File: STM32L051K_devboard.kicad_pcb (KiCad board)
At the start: 2 copper layers, 20.7 x 54.2 mm, 50 parts, among them J1 Conn_01x16_Pin, J2 Conn_01x16_Pin, J3 Conn_01x05_Pin, U1 STM32L051K8Ux

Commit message: cambios minimos
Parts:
- removed kibuzzard-69C45A72: G***, kibuzzard-69C45A72
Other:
- board text added: "STM32L051K8U"
- board text added: "X"

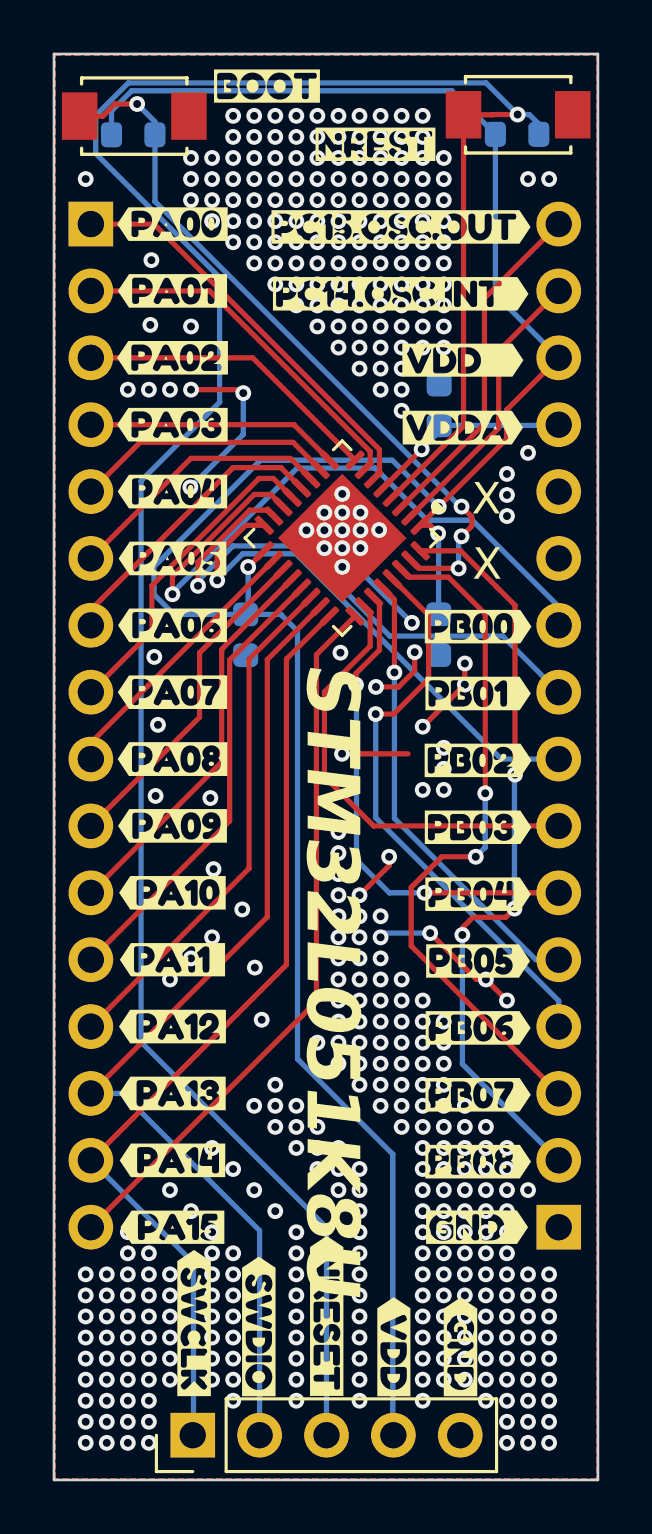
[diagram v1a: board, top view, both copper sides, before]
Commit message: Agregado XTAL low power y pines clock removidos
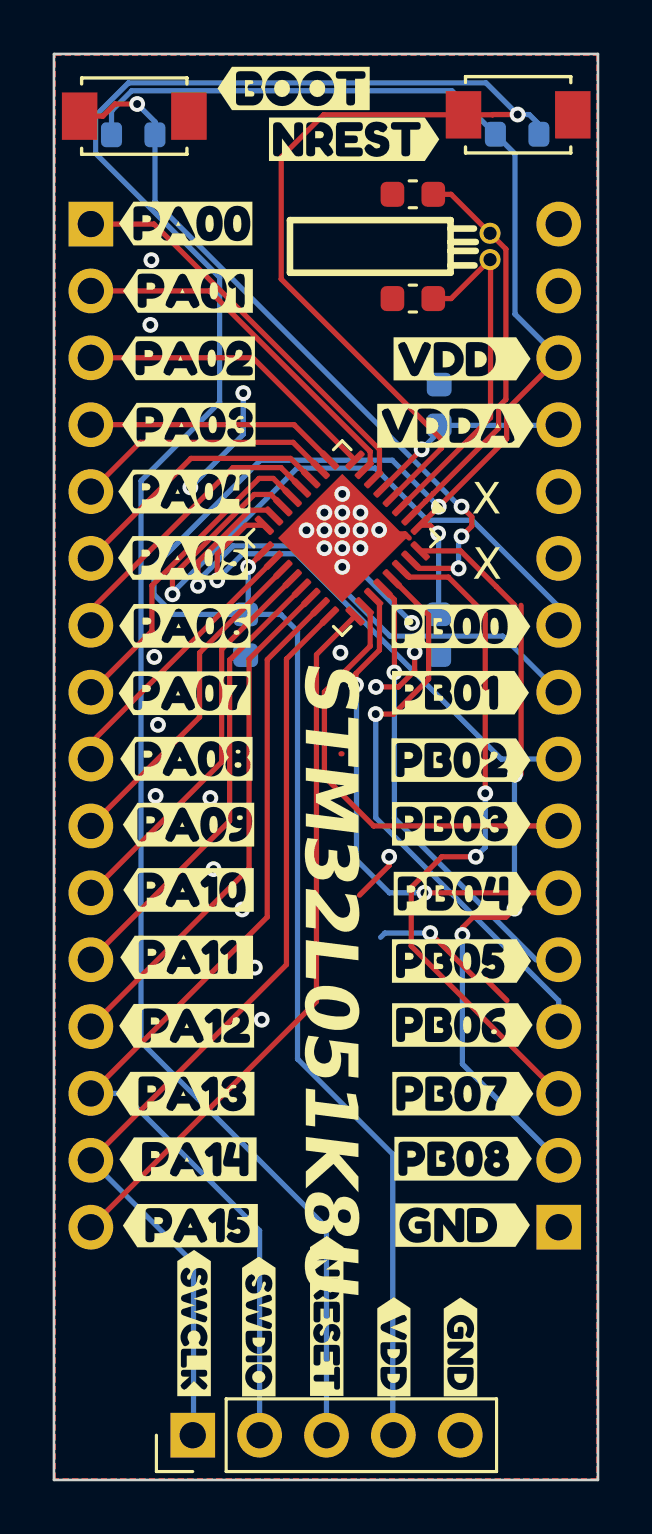
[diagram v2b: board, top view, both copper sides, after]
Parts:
- removed G***: LOGO, Images:LOGOv3.4
- removed kibuzzard-69C44E8F: G***, kibuzzard-69C44E8F
- removed kibuzzard-69C44ECA: G***, kibuzzard-69C44ECA
- removed kibuzzard-69C44EF4: G***, kibuzzard-69C44EF4
- removed kibuzzard-69C44F15: G***, kibuzzard-69C44F15
- removed kibuzzard-69C44F1D: G***, kibuzzard-69C44F1D
- removed kibuzzard-69C44F22: G***, kibuzzard-69C44F22
- removed kibuzzard-69C44F28: G***, kibuzzard-69C44F28
- removed kibuzzard-69C44FA1: G***, kibuzzard-69C44FA1
- removed kibuzzard-69C44FA7: G***, kibuzzard-69C44FA7
- removed kibuzzard-69C44FAD: G***, kibuzzard-69C44FAD
- removed kibuzzard-69C44FBD: G***, kibuzzard-69C44FBD
- removed kibuzzard-69C44FDE: G***, kibuzzard-69C44FDE
- removed kibuzzard-69C44FFF: G***, kibuzzard-69C44FFF
- removed kibuzzard-69C45005: G***, kibuzzard-69C45005
- removed kibuzzard-69C4500C: G***, kibuzzard-69C4500C
- removed kibuzzard-69C45011: G***, kibuzzard-69C45011
- removed kibuzzard-69C4505F: G***, kibuzzard-69C4505F
- removed kibuzzard-69C4508C: G***, kibuzzard-69C4508C
- removed kibuzzard-69C450DF: G***, kibuzzard-69C450DF
- removed kibuzzard-69C450F7: G***, kibuzzard-69C450F7
- removed kibuzzard-69C450FE: G***, kibuzzard-69C450FE
- removed kibuzzard-69C45105: G***, kibuzzard-69C45105
- removed kibuzzard-69C4510A: G***, kibuzzard-69C4510A
- removed kibuzzard-69C45110: G***, kibuzzard-69C45110
- removed kibuzzard-69C45115: G***, kibuzzard-69C45115
- removed kibuzzard-69C451D3: G***, kibuzzard-69C451D3
- removed kibuzzard-69C451DA: G***, kibuzzard-69C451DA
- removed kibuzzard-69C45252: G***, kibuzzard-69C45252
- removed kibuzzard-69C45274: G***, kibuzzard-69C45274
- removed kibuzzard-69C45C41: G***, kibuzzard-69C45C41
- removed kibuzzard-69C45C6A: G***, kibuzzard-69C45C6A
- removed kibuzzard-69C474E9: G***, kibuzzard-69C474E9
- added C1: 12pF, Capacitor_SMD:C_0603_1608Metric, F.Cu at (143.2, 77.4)
- added C2: 12pF, Capacitor_SMD:C_0603_1608Metric, F.Cu at (143.2, 73.5)
- added X1: TAXD32768K2BGBBZT2S, EasyEDA:OSC-TH_BD2.0-P0.70-D0.3, F.Cu at (146.1, 75.4)
- added kibuzzard-6A013291: G***, kibuzzard-6A013291, F.Cu at (134.5, 87.3)
- added kibuzzard-6A0132A3: G***, kibuzzard-6A0132A3, F.Cu at (134.5, 84.7)
- added kibuzzard-6A0132D3: G***, kibuzzard-6A0132D3, F.Cu at (134.6, 74.6)
- added kibuzzard-6A0132E0: G***, kibuzzard-6A0132E0, F.Cu at (134.7, 77.1)
- added kibuzzard-6A0132F9: G***, kibuzzard-6A0132F9, F.Cu at (134.7, 79.7)
- added kibuzzard-6A01330E: G***, kibuzzard-6A01330E, F.Cu at (134.7, 82.2)
- added kibuzzard-6A013338: G***, kibuzzard-6A013338, F.Cu at (134.5, 89.8)
- added kibuzzard-6A01335E: G***, kibuzzard-6A01335E, F.Cu at (134.5, 92.4)
- added kibuzzard-6A0133A5: G***, kibuzzard-6A0133A5, F.Cu at (134.6, 94.9)
- added kibuzzard-6A0133D4: G***, kibuzzard-6A0133D4, F.Cu at (134.7, 97.4)
- added kibuzzard-6A0133F3: G***, kibuzzard-6A0133F3, F.Cu at (134.7, 99.9)
- added kibuzzard-6A013428: G***, kibuzzard-6A013428, F.Cu at (134.6, 102.4)
- added kibuzzard-6A013453: G***, kibuzzard-6A013453, F.Cu at (134.6, 105.0)
- added kibuzzard-6A01346E: G***, kibuzzard-6A01346E, F.Cu at (134.6, 107.6)
- added kibuzzard-6A01348C: G***, kibuzzard-6A01348C, F.Cu at (134.7, 110.1)
- added kibuzzard-6A013498: G***, kibuzzard-6A013498, F.Cu at (134.8, 112.6)
- added kibuzzard-6A0134D7: G***, kibuzzard-6A0134D7, F.Cu at (145.1, 110.1)
- added kibuzzard-6A013521: G***, kibuzzard-6A013521, F.Cu at (138.7, 69.4)
- added kibuzzard-6A01353B: G***, kibuzzard-6A01353B, F.Cu at (141.0, 71.4)
- added kibuzzard-6A013575: G***, kibuzzard-6A013575, F.Cu at (145.1, 112.6)
- added kibuzzard-6A013597: G***, kibuzzard-6A013597, F.Cu at (145.1, 107.6)
- added kibuzzard-6A0135B5: G***, kibuzzard-6A0135B5, F.Cu at (145.1, 105.0)
- added kibuzzard-6A0135C4: G***, kibuzzard-6A0135C4, F.Cu at (145.1, 102.6)
- added kibuzzard-6A0135ED: G***, kibuzzard-6A0135ED, F.Cu at (145.0, 97.4)
- added kibuzzard-6A0135F3: G***, kibuzzard-6A0135F3, F.Cu at (145.1, 100.0)
- added kibuzzard-6A013611: G***, kibuzzard-6A013611, F.Cu at (145.0, 94.9)
- added kibuzzard-6A01362E: G***, kibuzzard-6A01362E, F.Cu at (145.0, 92.4)
- added kibuzzard-6A01363E: G***, kibuzzard-6A01363E, F.Cu at (145.0, 89.9)
- added kibuzzard-6A01366B: G***, kibuzzard-6A01366B, F.Cu at (144.8, 82.2)
- added kibuzzard-6A0136A4: G***, kibuzzard-6A0136A4, F.Cu at (145.1, 79.7)
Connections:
- J2 pad 15: /PC14_OSC.INT -> unconnected-(J2-Pin_15-Pad15)
- J2 pad 16: /PC15_OSC.OUT -> unconnected-(J2-Pin_16-Pad16)
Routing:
- net /NRST: track 92.3 -> 100.5 mm
- net GND: track 26.0 -> 20.6 mm, vias 426 -> 31
- net /PC14_OSC.INT: track 10.9 -> 15.3 mm
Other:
- board text added: "32.768 kHz"

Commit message: agregado LDO y VDDA puenteado a 3.3
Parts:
- removed kibuzzard-6A01366B: G***, kibuzzard-6A01366B
- removed kibuzzard-6A0136A4: G***, kibuzzard-6A0136A4
- added U2: XC6206P332MR, EasyEDA:SOT-23-3_L2.9-W1.6-P1.90-LS2.8-BR, B.Cu at (142.4, 75.7)
- added kibuzzard-6A120E41: G***, kibuzzard-6A120E41, F.Cu at (145.3, 82.2)
- added kibuzzard-6A120E83: G***, kibuzzard-6A120E83, F.Cu at (145.3, 79.7)
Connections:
- C4 pad 1: /VDDA -> /VDD0
- J2 pad 13: /VDDA -> /LDO
- U1 pad 5: /VDDA -> /VDD0
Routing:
- net /VDD0: track 93.8 -> 103.7 mm, vias 3 -> 4
- net /LDO: track 0.00 -> 8.62 mm
- net /VDDA: track 7.82 -> 0.00 mm, vias 1 -> 0
- net GND: vias 31 -> 277

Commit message: cambio de crital a SMD 8 MHz
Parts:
- removed X1: TAXD32768K2BGBBZT2S, EasyEDA:OSC-TH_BD2.0-P0.70-D0.3
- removed kibuzzard-6A013575: G***, kibuzzard-6A013575
- added D1: LED_Small, LED_SMD:LED_0603_1608Metric, F.Cu at (140.7, 79.5)
- added D2: LED_Small, LED_SMD:LED_0603_1608Metric, F.Cu at (131.8, 115.9)
- added JP1: SolderJumper_2_Open, Jumper:SolderJumper-2_P1.3mm_Open_TrianglePad1.0x1.5mm, B.Cu at (135.5, 72.0)
- added JP2: SolderJumper_2_Open, Jumper:SolderJumper-2_P1.3mm_Open_TrianglePad1.0x1.5mm, B.Cu at (131.5, 119.6)
- added R3: 4.7k, Resistor_SMD:R_0603_1608Metric, B.Cu at (138.8, 71.2)
- added R4: 4.7k, Resistor_SMD:R_0603_1608Metric, B.Cu at (131.0, 116.1)
- added X2: X32258MOB4SI, EasyEDA:CRYSTAL-SMD_4P-L3.2-W2.5-BL, F.Cu at (143.4, 75.0)
- moved C1 4.96 mm to (139.5, 74.2)
- moved C2 4.44 mm to (139.5, 75.8)
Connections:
- C1 pad 1: /PC15_OSC.OUT -> /PC14_OSC.INT
- C2 pad 1: /PC14_OSC.INT -> /PC15_OSC.OUT
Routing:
- net Net-(D1-A): track 0.00 -> 9.06 mm, vias 0 -> 1
- net Net-(D1-K): track 0.00 -> 8.52 mm, vias 0 -> 1
- net /NRST: track 100.5 -> 105.6 mm
- net /PC14_OSC.INT: track 15.3 -> 20.4 mm
- net Net-(D2-A): track 0.00 -> 4.66 mm, vias 0 -> 1
- net Net-(D2-K): track 0.00 -> 3.51 mm, vias 0 -> 1
- net /PA15: track 27.4 -> 30.0 mm
- net /VDD0: track 103.7 -> 105.6 mm, vias 4 -> 5
- net GND: vias 277 -> 237
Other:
- board text added: "+"
- board text added: "Power"
- board text added: "test"
- board text added: "test jumper"
- board text removed: "32.768 kHz"

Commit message: agregado 4 capas y relleno
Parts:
- removed kibuzzard-6A120E83: G***, kibuzzard-6A120E83
- added kibuzzard-6A389A11: G***, kibuzzard-6A389A11, F.Cu at (145.3, 79.7)
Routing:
- added copper zone on In1.Cu, net GND
- added copper zone on In2.Cu, net GND
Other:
- copper layers 2 -> 4
